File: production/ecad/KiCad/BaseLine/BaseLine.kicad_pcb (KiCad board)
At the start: 2 copper layers, 124 parts, among them IC1 AP7362-33SP-13 (3.3V LDO), J1 VibeMotorConnector_1, J10 LoadCell1, J11 LoadCell2, J12 LoadCell3, J13 LoadCell4, J14 Power_to_Loadcell, J17 IMU_connector, J2 1332645, J3 Conn_01x02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

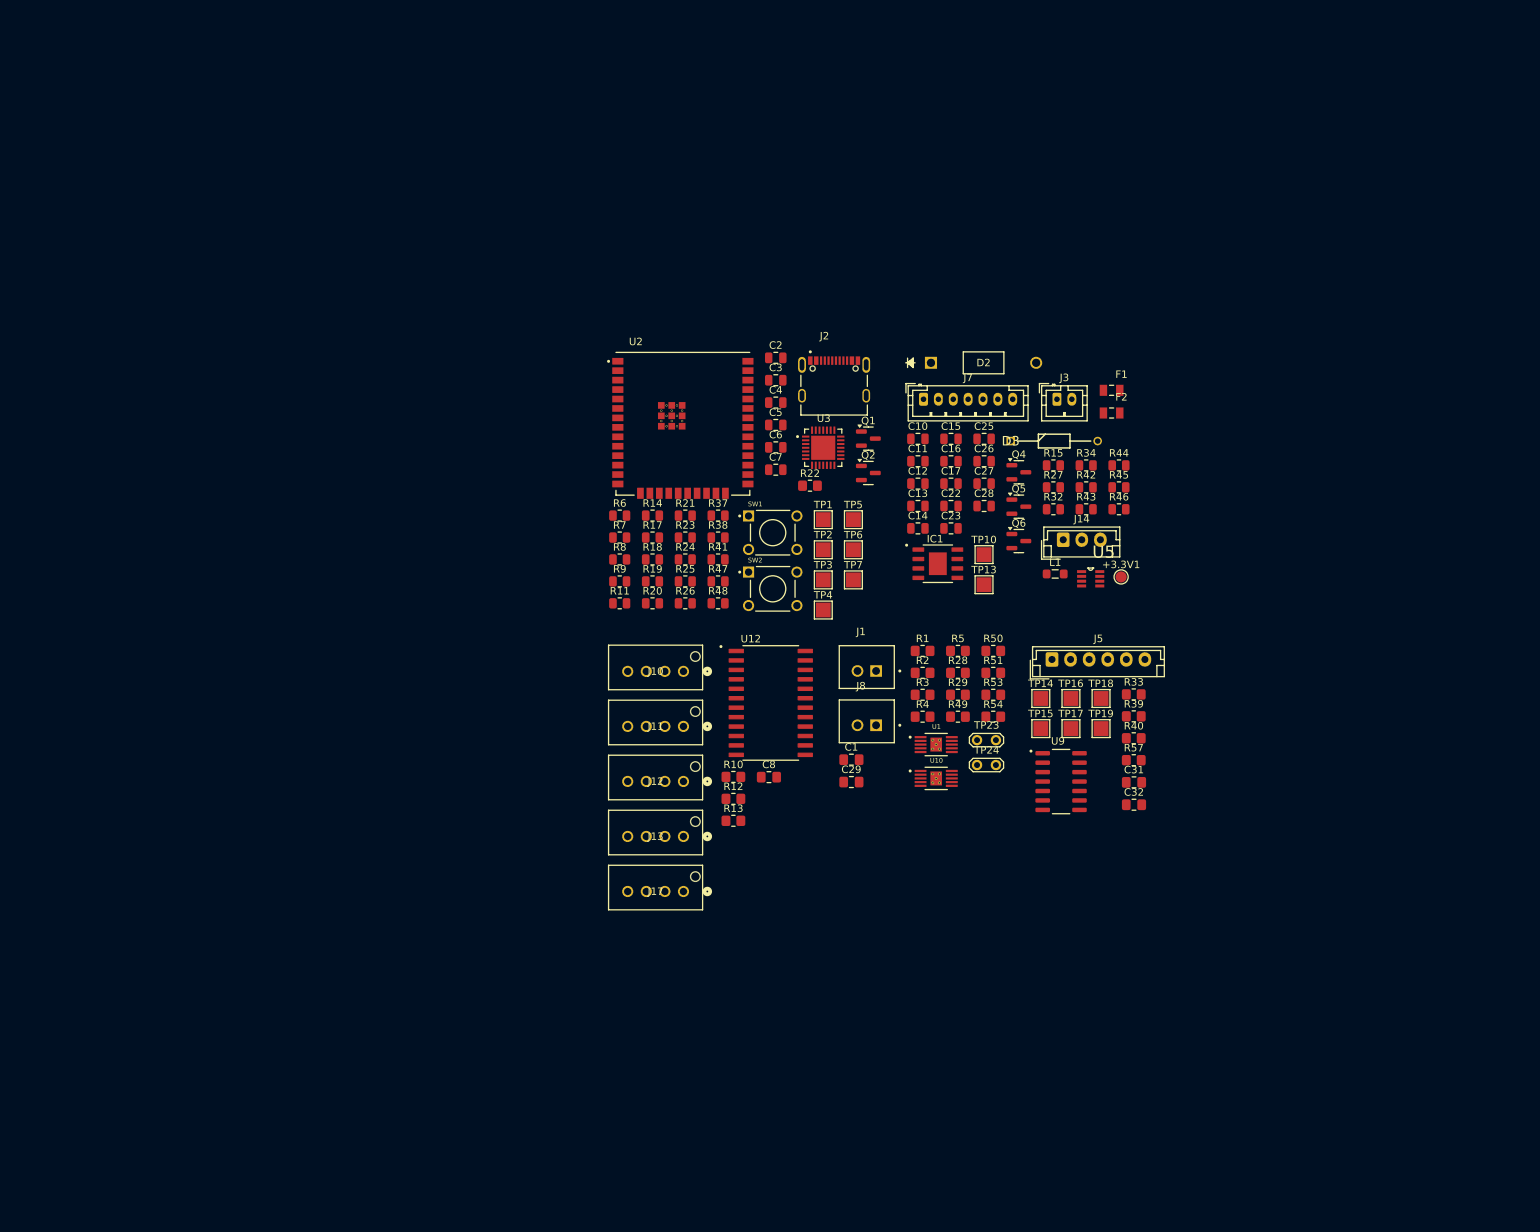
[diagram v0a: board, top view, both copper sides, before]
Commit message: Microcontroller changes on layout
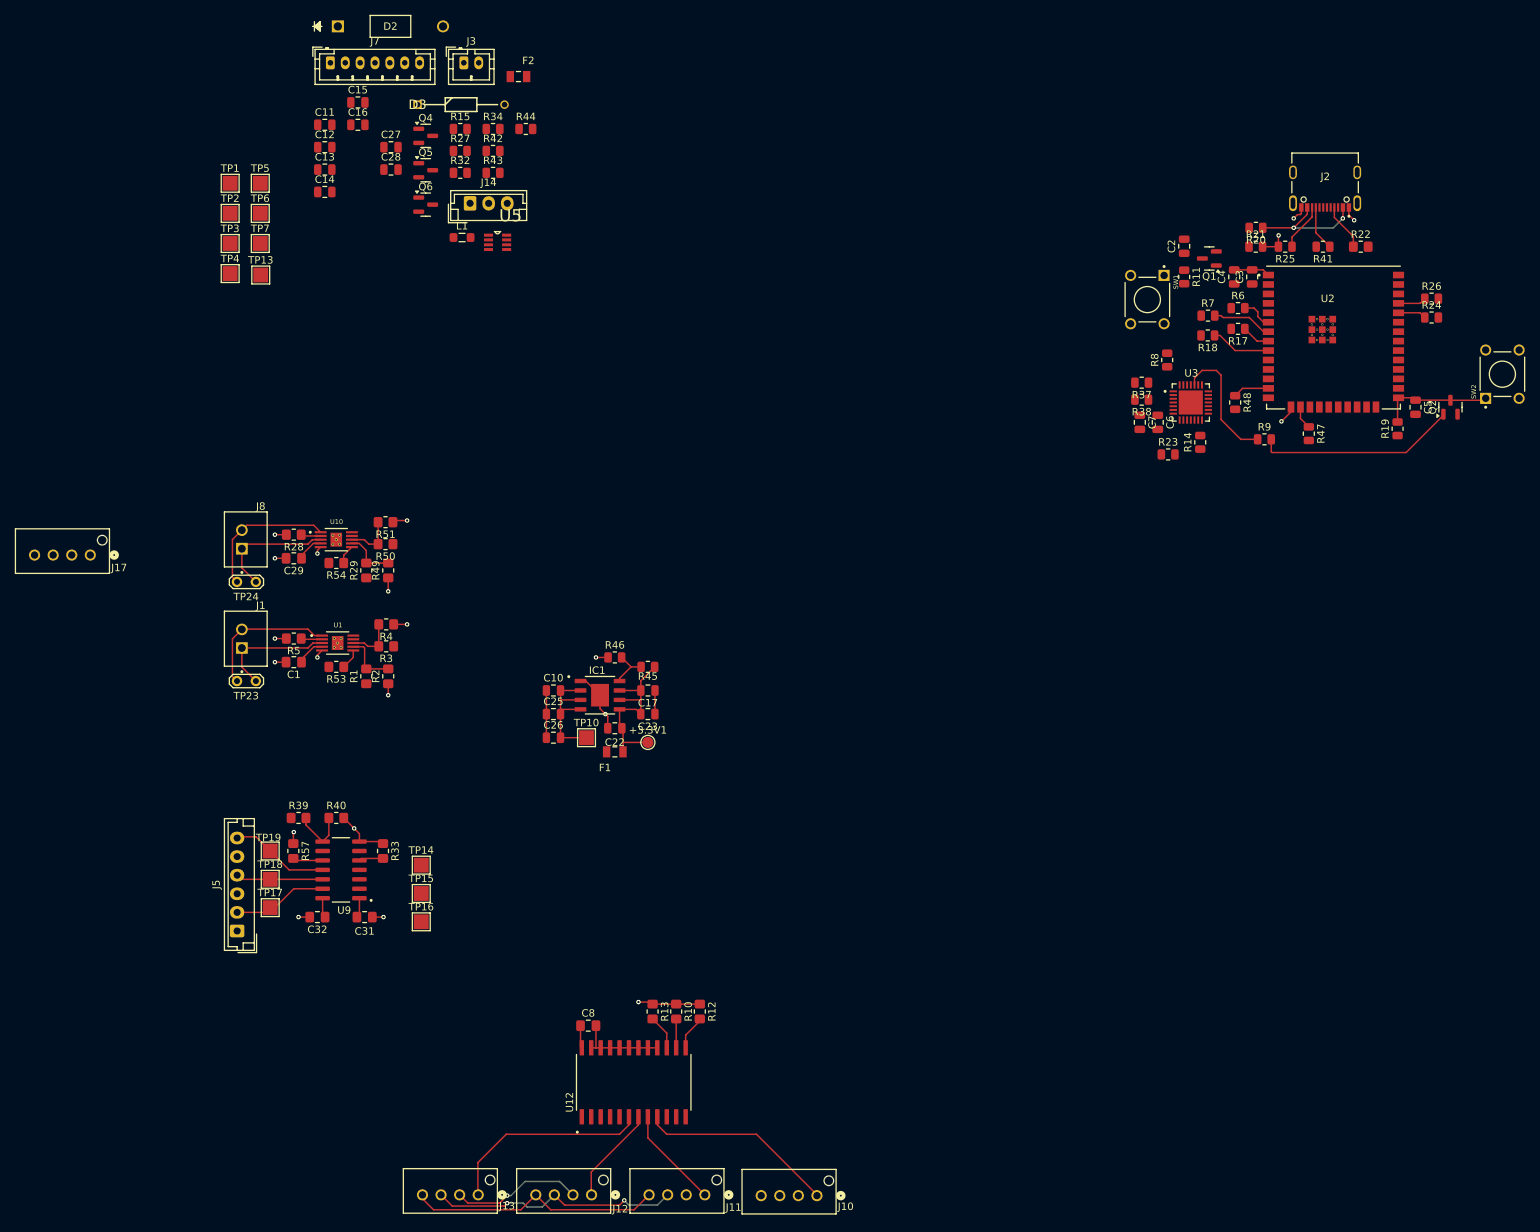
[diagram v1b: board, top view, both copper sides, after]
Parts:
- moved J5 115.5 mm to (57.8, 144.7), turned to 90 degrees
- moved TP18 114.4 mm to (62.2, 137.8)
- moved R57 113.7 mm to (65.3, 134.0), turned to -90 degrees
- moved R39 113.2 mm to (66.0, 129.5)
- moved TP19 113.0 mm to (62.2, 134.0)
- moved C32 110.9 mm to (68.6, 142.9), turned to 180 degrees
- moved TP17 110.4 mm to (62.2, 141.6)
- moved R26 108.4 mm to (218.4, 59.7)
- moved R40 107.8 mm to (71.1, 129.5)
- moved TP13 105.8 mm to (61.0, 56.5)
- moved R24 105.5 mm to (218.4, 62.2)
- moved C31 105.1 mm to (74.9, 142.9)
- moved R33 103.2 mm to (77.4, 134.0), turned to -90 degrees
- moved SW2 102.3 mm to (228.0, 69.8), turned to 90 degrees
- moved R19 102.3 mm to (213.9, 77.2), turned to 90 degrees
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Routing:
- net GND: track 0.00 -> 82.3 mm, vias 0 -> 21
- net SPEED: track 0.00 -> 34.1 mm
- net PDWN: track 0.00 -> 33.8 mm, vias 0 -> 2
- net DOUT_3: track 0.00 -> 27.9 mm
- net Net-(Q2-G): track 0.00 -> 27.1 mm
- net DOUT_0: track 0.00 -> 26.6 mm
- net Net-(IC1-OUT_1): track 0.00 -> 25.2 mm
- net Net-(J8-Pin_2): track 0.00 -> 19.0 mm
- net Net-(J1-Pin_2): track 0.00 -> 18.5 mm
- net +3.7V: track 0.00 -> 17.9 mm
- net CLK: track 0.00 -> 17.6 mm, vias 0 -> 1
- net RTS: track 0.00 -> 17.2 mm
- net Net-(J8-Pin_1): track 0.00 -> 16.3 mm
- net VBUS: track 0.00 -> 16.3 mm, vias 0 -> 2
- net Net-(J1-Pin_1): track 0.00 -> 15.9 mm
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- added copper zone on In2.Cu, net GND
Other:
- copper layers 2 -> 4

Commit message: doing some things for layout
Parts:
- moved J17 181.1 mm to (218.2, 112.0)
- moved C31 0.14 mm to (75.0, 143.0), turned to 180 degrees
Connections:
- C31 pad 1: +3.3V -> GND
- C31 pad 2: GND -> +3.3V
- C8 pad 2: GND -> Net-(U12-VCC)
- U12 pad 24: +5V -> Net-(U12-VCC)
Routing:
- net CLK: track 17.6 -> 55.3 mm
- net PDWN: track 33.8 -> 51.7 mm
- net SPEED: track 34.1 -> 51.5 mm
- net GND: track 82.3 -> 86.3 mm, vias 21 -> 23

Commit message: PCB changes
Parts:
- moved J2 53.3 mm to (157.8, 56.1), turned to -90 degrees
- moved J17 48.9 mm to (187.2, 74.2), turned to 180 degrees
- moved R22 38.7 mm to (170.4, 55.8), turned to 90 degrees
- moved R41 35.9 mm to (169.2, 62.0), turned to -90 degrees
- moved R20 33.4 mm to (167.8, 69.9), turned to -90 degrees
- moved R25 31.3 mm to (170.4, 65.9), turned to -90 degrees
- moved R21 29.9 mm to (170.4, 69.9), turned to 90 degrees
- moved R14 11.4 mm to (182.2, 68.9)
- moved R18 11.2 mm to (183.7, 54.5)
- moved R6 11.2 mm to (187.8, 50.8)
- moved C3 11.2 mm to (189.7, 46.6)
- moved C5 11.2 mm to (211.7, 64.1)
- moved C6 11.2 mm to (177.0, 66.2)
- moved C7 11.2 mm to (174.6, 66.2)
- moved Q1 11.2 mm to (183.9, 44.1)
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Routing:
- net GND: track 86.3 -> 135.3 mm, vias 23 -> 27
- net +3.3V: track 2.78 -> 40.0 mm, vias 0 -> 1
- net RTS: track 17.2 -> 38.9 mm, vias 0 -> 2
- net Net-(Q1-G): track 0.00 -> 15.3 mm, vias 0 -> 2
- net Net-(U3-VBUS): track 0.00 -> 15.2 mm
- net SCL: track 4.88 -> 17.6 mm, vias 0 -> 1
- net SDA: track 3.13 -> 13.2 mm, vias 0 -> 1
- net EN: track 0.00 -> 7.99 mm
- net Net-(U3-~{RST}): track 0.00 -> 5.10 mm
- net Net-(U3-D+): track 0.00 -> 4.96 mm
- net Net-(U3-D-): track 0.00 -> 3.70 mm
- net DTR: track 0.00 -> 3.14 mm
- net Net-(U3-~{SUSPEND}): track 0.00 -> 2.41 mm
- net Net-(J2-SBU1): track 6.06 -> 4.38 mm

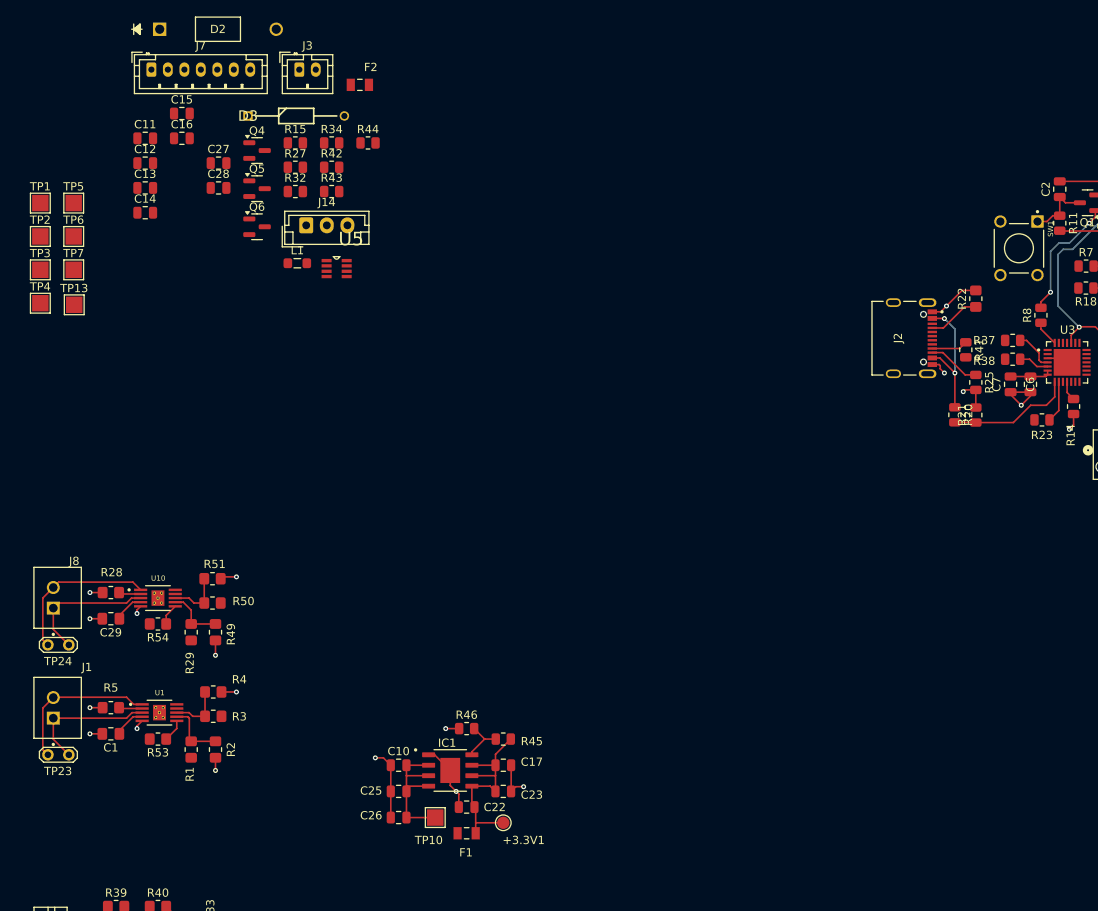
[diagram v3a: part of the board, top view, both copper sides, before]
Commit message: Added Battery e-stop, 5V boost and moved the 3.3V to the layout
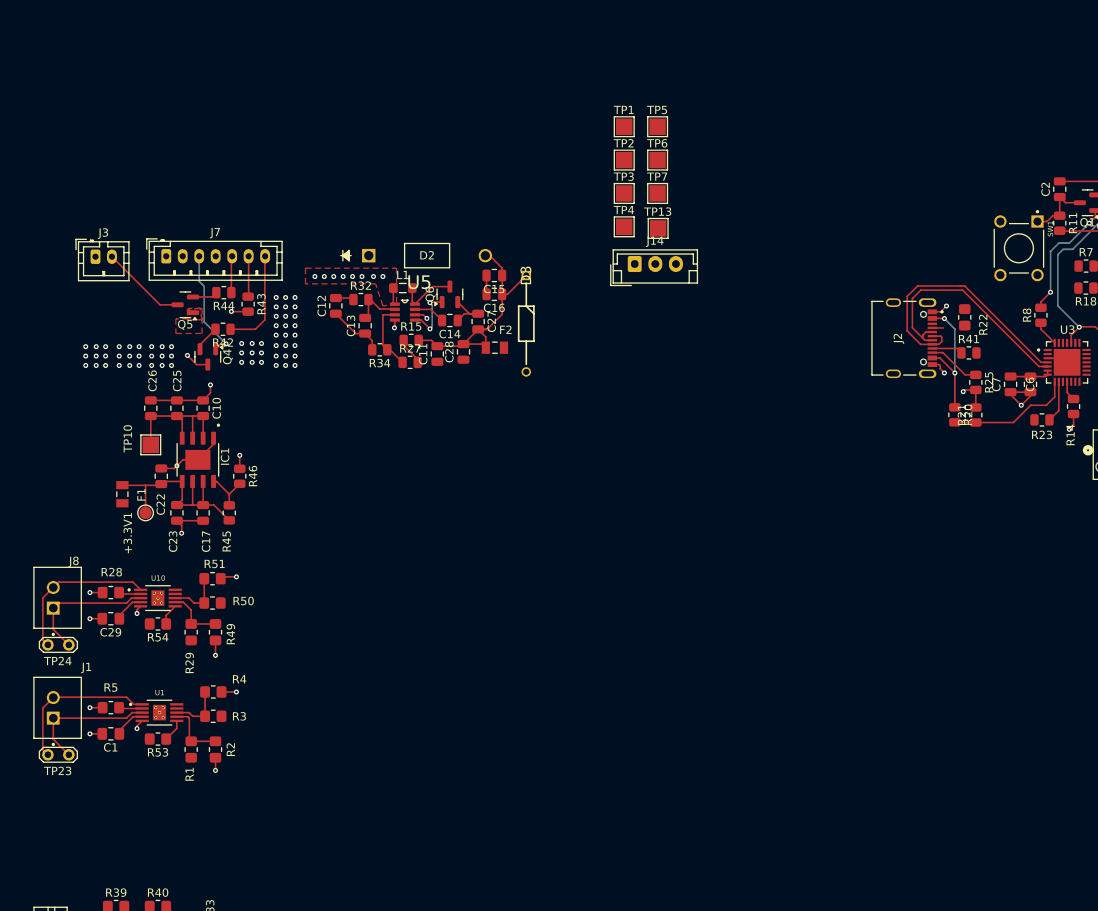
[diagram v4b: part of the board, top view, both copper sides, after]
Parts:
- removed R37, R38: 0, Resistor_SMD:R_0805_2012Metric
- moved TP1 71.5 mm to (127.7, 34.9)
- moved TP2 71.5 mm to (127.7, 38.9)
- moved TP3 71.5 mm to (127.7, 43.0)
- moved TP4 71.5 mm to (127.7, 47.0)
- moved TP13 71.5 mm to (131.8, 47.2)
- moved TP5 71.5 mm to (131.8, 34.9)
- moved TP6 71.5 mm to (131.8, 38.9)
- moved TP7 71.5 mm to (131.8, 43.0)
- moved F1 58.6 mm to (66.8, 79.5), turned to -90 degrees
- moved C26 58.1 mm to (70.3, 69.1), turned to -90 degrees
- moved +3.3V1 57.4 mm to (69.6, 81.8), turned to -90 degrees
- moved TP10 56.9 mm to (70.3, 73.5), turned to -90 degrees
- moved C22 54.6 mm to (71.5, 77.3), turned to -90 degrees
- moved C25 53.7 mm to (73.4, 69.1), turned to -90 degrees
- moved C23 52.1 mm to (73.4, 81.8), turned to 90 degrees
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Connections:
- J3 pad 1: Net-(J3-Pin_1) -> +3.7V
- J7 pad 1: Net-(J3-Pin_1) -> +3.7V
- J7 pad 4: Net-(J3-Pin_1) -> +3.7V
- U3 pad 4: Net-(U3-D+) -> USB_D+
- U3 pad 5: Net-(U3-D-) -> USB_D-
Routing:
- net USB_D+: track 0.00 -> 32.3 mm
- net Net-(D2A-K): track 0.00 -> 31.8 mm
- net USB_D-: track 0.00 -> 29.6 mm
- net GND: track 135.3 -> 162.8 mm, vias 27 -> 30
- net Net-(J7-Pin_3): track 0.00 -> 13.5 mm, vias 0 -> 1
- net Net-(J7-Pin_7): track 0.00 -> 12.4 mm
- net Net-(U5-VFB): track 0.00 -> 8.37 mm
- net Net-(Q6-G): track 0.00 -> 7.53 mm, vias 0 -> 2
- net Net-(D2A-A): track 0.00 -> 7.21 mm
- net Net-(U5-ITH): track 0.00 -> 6.09 mm
- net Net-(J2-CC1): track 6.34 -> 1.35 mm
- net Net-(U3-D+): track 4.96 -> 0.00 mm
- net Net-(J7-Pin_6): track 0.00 -> 4.92 mm
- net Net-(J7-Pin_5): track 0.00 -> 4.45 mm
- net +3.7V: track 17.9 -> 21.9 mm, vias 0 -> 69
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- added copper zone on F.Cu, net +3.7V
- added copper zone on In1.Cu, net +3.7V
